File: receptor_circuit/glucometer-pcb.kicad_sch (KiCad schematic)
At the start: 22 parts, among them IC1 RC4558IP, IC2 LM1458N, IC3 RC4558IP, U1 ESP32_DevKit_V1_DOIT

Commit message: change name
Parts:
- removed BZ1: Buzzer, Buzzer_Beeper:MagneticBuzzer_Kingstate_KCG0601, symbol Device:Buzzer
- removed D1: LED, LED_THT:LED_D3.0mm_Clear, symbol Device:LED
- removed D2: LED, LED_THT:LED_D3.0mm_FlatTop, symbol Device:LED
- removed R3: 120, Resistor_THT:R_Axial_DIN0204_L3.6mm_D1.6mm_P7.62mm_Horizontal, symbol Device:R
- removed R4: 240, Resistor_THT:R_Axial_DIN0204_L3.6mm_D1.6mm_P7.62mm_Horizontal, symbol Device:R
- removed U1: ESP32_DevKit_V1_DOIT, esp32_devkit_v1_doit:esp32_devkit_v1_doit, symbol esp32_devkit_v1_doit:ESP32_DevKit_V1_DOIT
- added TP3: (no value), TestPoint:TestPoint_Keystone_5015_Micro-Minature, symbol Connector:TestPoint
- renumbered D3 to D1, R5 to R3, R6 to R4, R7 to R5, R8 to R6, R9 to R7
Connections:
- net SIGNAL_OUT: no longer names the net of IC3.6 (2IN-), R6.1, R7.2
- net SIGNAL_OUT: now also TP3.1

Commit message: fixed PCB
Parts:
- LM1458N1: renamed from IC2; value LM1458N -> (none)
- S_OUT1: renamed from TP3; footprint TestPoint:TestPoint_Keystone_5015_Micro-Minature -> (none)
- renumbered C2 to C1, C3 to C2, C1 to C3, TP1 to GND1, R4 to R1, R5 to R2, R1 to R3, R2 to R4, R3 to R5, IC1 to RC4558IP1, IC3 to RC4558IP2, D1 to RECEPTOR_DIODE1, TP2 to VCC1
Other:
- moved on the sheet: C1, C2, C3, GND1, LM1458N1, R1, R2, R3, R4, R5, R6, R7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

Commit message: receptor footprint update
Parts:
- LM1458N1: value (none) -> LM1458N
- RECEPTOR_DIODE1: footprint LED_SMD:LED_2010_5025Metric -> (none)
- S_OUT1: value (none) -> SIGNAL_OUT; footprint (none) -> TestPoint:TestPoint_Keystone_5015_Micro-Minature
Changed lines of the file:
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@@
       (effects (font (size 1.27 1.27)) (justify left))
     )
-    (property "Value" "" (id 1) (at 270.8694 62.425 90)
-      (effects (font (size 1.27 1.27)) (justify left))
-    )
-    (property "Footprint" "" (id 2) (at 265.7894 66.2351 0)
+    (property "Value" "SIGNAL_OUT" (id 1) (at 270.8694 62.425 90)
+      (effects (font (size 1.27 1.27)) (justify left))
+    )
+    (property "Footprint" "TestPoint:TestPoint_Keystone_5015_Micro-Minature" (id 2) (at 265.7894 66.2351 0)
       (effects (font (size 1.27 1.27)) hide)
     )
@@
     (in_bom yes) (on_board yes) (fields_autoplaced)
     (property "Reference" "LM1458N1" (id 0) (at 76.2 58.42 0))
-    (property "Value" "" (id 1) (at 76.2 60.96 0))
+    (property "Value" "LM1458N" (id 1) (at 76.2 60.96 0))
     (property "Footprint" "Custom:MC1458N" (id 2) (at 107.95 63.5 0)
       (effects (font (size 1.27 1.27)) (justify left) hide)
@@
       (effects (font (size 1.27 1.27)) (justify right))
     )
-    (property "Footprint" "LED_SMD:LED_2010_5025Metric" (id 2) (at 17.78 50.8 0)
+    (property "Footprint" "" (id 2) (at 17.78 50.8 0)
       (effects (font (size 1.27 1.27)) hide)
     )
@@
     )
     (path "/e278b743-dbab-45ed-8e87-8cb90b916702"
-      (reference "RECEPTOR_DIODE1") (unit 1) (value "D_Photo") (footprint "LED_SMD:LED_2010_5025Metric")
+      (reference "RECEPTOR_DIODE1") (unit 1) (value "D_Photo") (footprint "LED_SMD:LED_2512_6332Metric")
     )
     (path "/34600403-f41d-47ed-8742-771add37111a"

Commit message: updated footprints
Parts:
- C1: value 15p -> (none); footprint Capacitor_THT:CP_Radial_D8.0mm_P3.80mm -> (none)
- C2: value 100n -> (none); footprint Capacitor_THT:CP_Radial_Tantal_D7.0mm_P5.00mm -> (none)
- C3: value 10u -> (none); footprint Capacitor_THT:CP_Radial_Tantal_D7.0mm_P5.00mm -> (none)
- RECEPTOR_DIODE1: footprint (none) -> LED_SMD:LED_2512_6332Metric
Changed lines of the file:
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@@
     (in_bom yes) (on_board yes) (fields_autoplaced)
     (property "Reference" "C3" (id 0) (at 175.337 120.1313 90))
-    (property "Value" "10u" (id 1) (at 175.337 122.6713 90))
-    (property "Footprint" "Capacitor_THT:CP_Radial_Tantal_D7.0mm_P5.00mm" (id 2) (at 179.147 126.7861 0)
+    (property "Value" "" (id 1) (at 175.337 122.6713 90))
+    (property "Footprint" "" (id 2) (at 179.147 126.7861 0)
       (effects (font (size 1.27 1.27)) hide)
     )
@@
     (in_bom yes) (on_board yes) (fields_autoplaced)
     (property "Reference" "C1" (id 0) (at 44.45 24.13 90))
-    (property "Value" "15p" (id 1) (at 44.45 26.67 90))
-    (property "Footprint" "Capacitor_THT:CP_Radial_D8.0mm_P3.80mm" (id 2) (at 48.26 30.7848 0)
+    (property "Value" "" (id 1) (at 44.45 26.67 90))
+    (property "Footprint" "" (id 2) (at 48.26 30.7848 0)
       (effects (font (size 1.27 1.27)) hide)
     )
@@
       (effects (font (size 1.27 1.27)) (justify right))
     )
-    (property "Value" "100n" (id 1) (at 85.09 31.7499 0)
+    (property "Value" "" (id 1) (at 85.09 31.7499 0)
       (effects (font (size 1.27 1.27)) (justify right))
     )
-    (property "Footprint" "Capacitor_THT:CP_Radial_Tantal_D7.0mm_P5.00mm" (id 2) (at 107.95 25.4 0)
+    (property "Footprint" "" (id 2) (at 107.95 25.4 0)
       (effects (font (size 1.27 1.27)) hide)
     )
@@
       (effects (font (size 1.27 1.27)) (justify right))
     )
-    (property "Footprint" "" (id 2) (at 17.78 50.8 0)
+    (property "Footprint" "LED_SMD:LED_2512_6332Metric" (id 2) (at 17.78 50.8 0)
       (effects (font (size 1.27 1.27)) hide)
     )
@@
     )
     (path "/6e51d59d-a712-422e-a594-3a08db72143f"
-      (reference "C1") (unit 1) (value "15p") (footprint "Capacitor_THT:CP_Radial_D8.0mm_P3.80mm")
+      (reference "C1") (unit 1) (value "15p") (footprint "Capacitor_THT:C_Disc_D4.3mm_W1.9mm_P5.00mm")
     )
     (path "/8777605c-db0c-4cf4-9b07-6eb49a9a4f9e"
-      (reference "C2") (unit 1) (value "100n") (footprint "Capacitor_THT:CP_Radial_Tantal_D7.0mm_P5.00mm")
+      (reference "C2") (unit 1) (value "100n") (footprint "Capacitor_THT:C_Disc_D4.3mm_W1.9mm_P5.00mm")
     )
     (path "/4a7b0df0-d7d6-445b-b3ac-9e0367190cc3"
-      (reference "C3") (unit 1) (value "10u") (footprint "Capacitor_THT:CP_Radial_Tantal_D7.0mm_P5.00mm")
+      (reference "C3") (unit 1) (value "10u") (footprint "Capacitor_THT:C_Disc_D4.3mm_W1.9mm_P5.00mm")
     )
     (path "/c1089e62-6a3d-4c09-9cdd-b0398d606cc7"

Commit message: .
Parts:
- C1: value (none) -> 15p; footprint (none) -> Capacitor_THT:C_Disc_D4.3mm_W1.9mm_P5.00mm
- C2: value (none) -> 100n; footprint (none) -> Capacitor_THT:C_Disc_D4.3mm_W1.9mm_P5.00mm
- C3: footprint (none) -> Capacitor_THT:C_Disc_D4.3mm_W1.9mm_P5.00mm
- R5: value 25k -> (none); footprint Resistor_THT:R_Axial_DIN0204_L3.6mm_D1.6mm_P7.62mm_Horizontal -> (none)
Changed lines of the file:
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@@
   (symbol (lib_id "Device:C") (at 175.337 127.7513 90) (unit 1)
     (in_bom yes) (on_board yes) (fields_autoplaced)
-    (property "Reference" "C3" (id 0) (at 175.337 120.1313 90))
-    (property "Value" "" (id 1) (at 175.337 122.6713 90))
-    (property "Footprint" "" (id 2) (at 179.147 126.7861 0)
+    (property "Reference" "C3" (id 0) (at 175.337 120.65 90))
+    (property "Value" "" (id 1) (at 175.337 123.19 90))
+    (property "Footprint" "Capacitor_THT:C_Disc_D4.3mm_W1.9mm_P5.00mm" (id 2) (at 179.147 126.7861 0)
       (effects (font (size 1.27 1.27)) hide)
     )
@@
       (effects (font (size 1.27 1.27)) (justify left))
     )
-    (property "Value" "25k" (id 1) (at 190.577 141.7212 0)
-      (effects (font (size 1.27 1.27)) (justify left))
-    )
-    (property "Footprint" "Resistor_THT:R_Axial_DIN0204_L3.6mm_D1.6mm_P7.62mm_Horizontal" (id 2) (at 186.259 140.4513 90)
+    (property "Value" "" (id 1) (at 190.577 141.7212 0)
+      (effects (font (size 1.27 1.27)) (justify left))
+    )
+    (property "Footprint" "" (id 2) (at 186.259 140.4513 90)
       (effects (font (size 1.27 1.27)) hide)
     )
@@
     (in_bom yes) (on_board yes) (fields_autoplaced)
     (property "Reference" "C1" (id 0) (at 44.45 24.13 90))
-    (property "Value" "" (id 1) (at 44.45 26.67 90))
-    (property "Footprint" "" (id 2) (at 48.26 30.7848 0)
+    (property "Value" "15p" (id 1) (at 44.45 26.67 90))
+    (property "Footprint" "Capacitor_THT:C_Disc_D4.3mm_W1.9mm_P5.00mm" (id 2) (at 48.26 30.7848 0)
       (effects (font (size 1.27 1.27)) hide)
     )
@@
       (effects (font (size 1.27 1.27)) (justify right))
     )
-    (property "Value" "" (id 1) (at 85.09 31.7499 0)
+    (property "Value" "100n" (id 1) (at 85.09 31.7499 0)
       (effects (font (size 1.27 1.27)) (justify right))
     )
-    (property "Footprint" "" (id 2) (at 107.95 25.4 0)
+    (property "Footprint" "Capacitor_THT:C_Disc_D4.3mm_W1.9mm_P5.00mm" (id 2) (at 107.95 25.4 0)
       (effects (font (size 1.27 1.27)) hide)
     )
@@
     )
     (path "/4a7b0df0-d7d6-445b-b3ac-9e0367190cc3"
-      (reference "C3") (unit 1) (value "10u") (footprint "Capacitor_THT:C_Disc_D4.3mm_W1.9mm_P5.00mm")
+      (reference "C3") (unit 1) (value "1u") (footprint "Capacitor_THT:C_Disc_D4.3mm_W1.9mm_P5.00mm")
     )
     (path "/c1089e62-6a3d-4c09-9cdd-b0398d606cc7"
@@
     )
     (path "/5e1aeaac-5127-4872-a12f-e8e4419955ab"
-      (reference "R5") (unit 1) (value "25k") (footprint "Resistor_THT:R_Axial_DIN0204_L3.6mm_D1.6mm_P7.62mm_Horizontal")
+      (reference "R5") (unit 1) (value "300k") (footprint "Resistor_THT:R_Axial_DIN0204_L3.6mm_D1.6mm_P7.62mm_Horizontal")
     )
     (path "/21328896-da89-4b46-b5e9-10fe97839bf4"

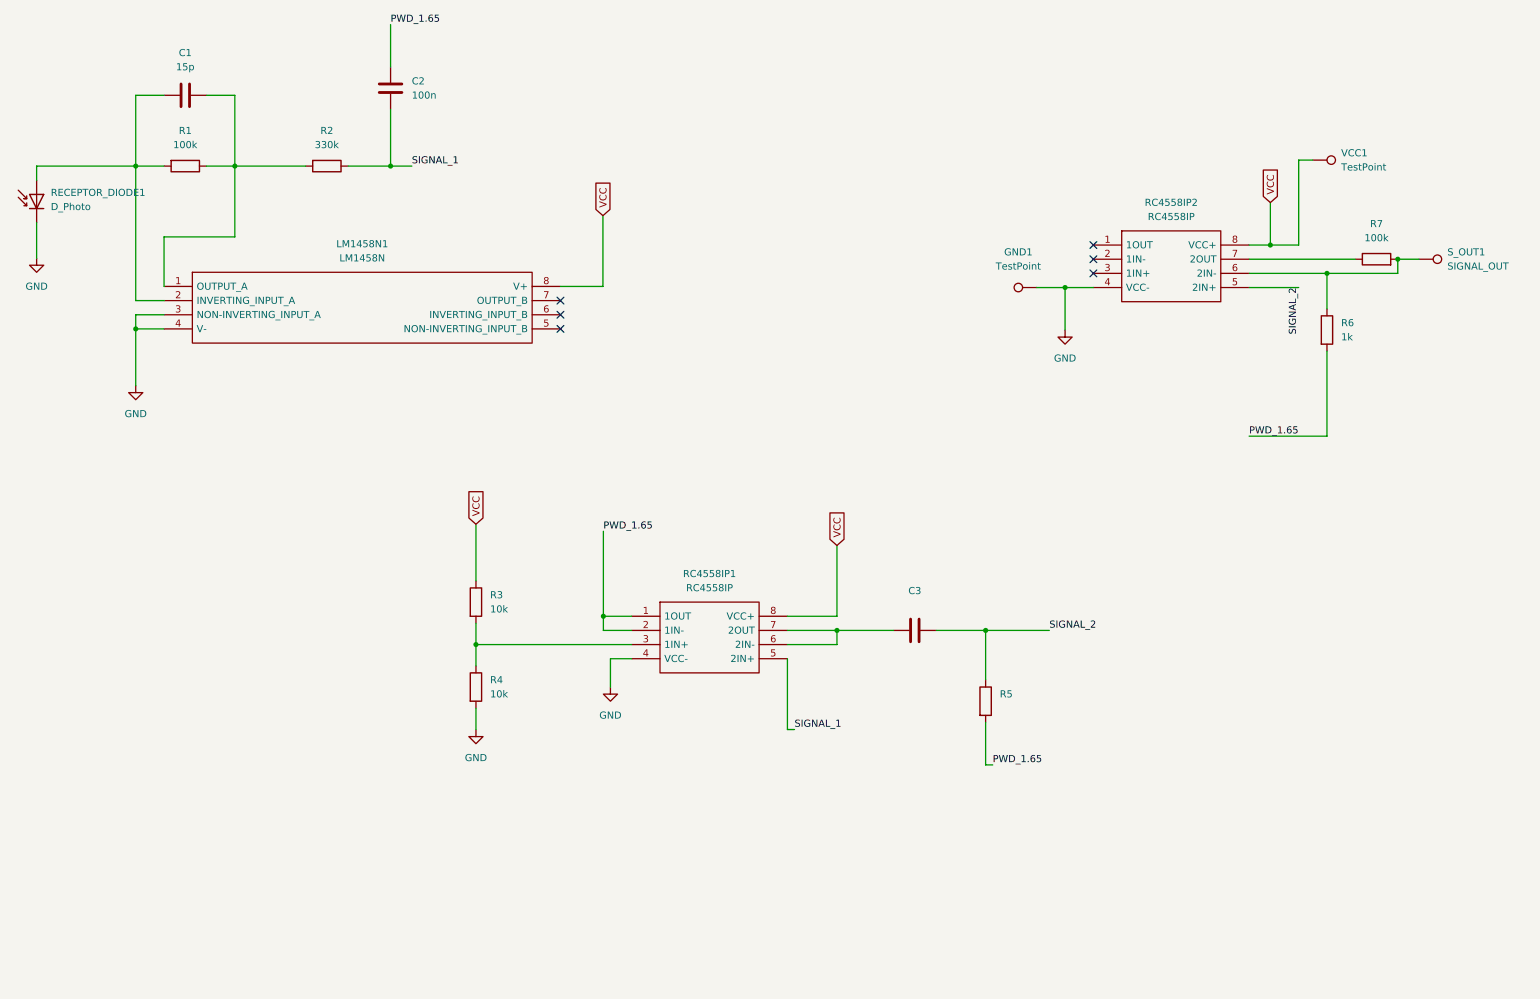
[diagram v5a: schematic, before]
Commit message: updated pcb pads
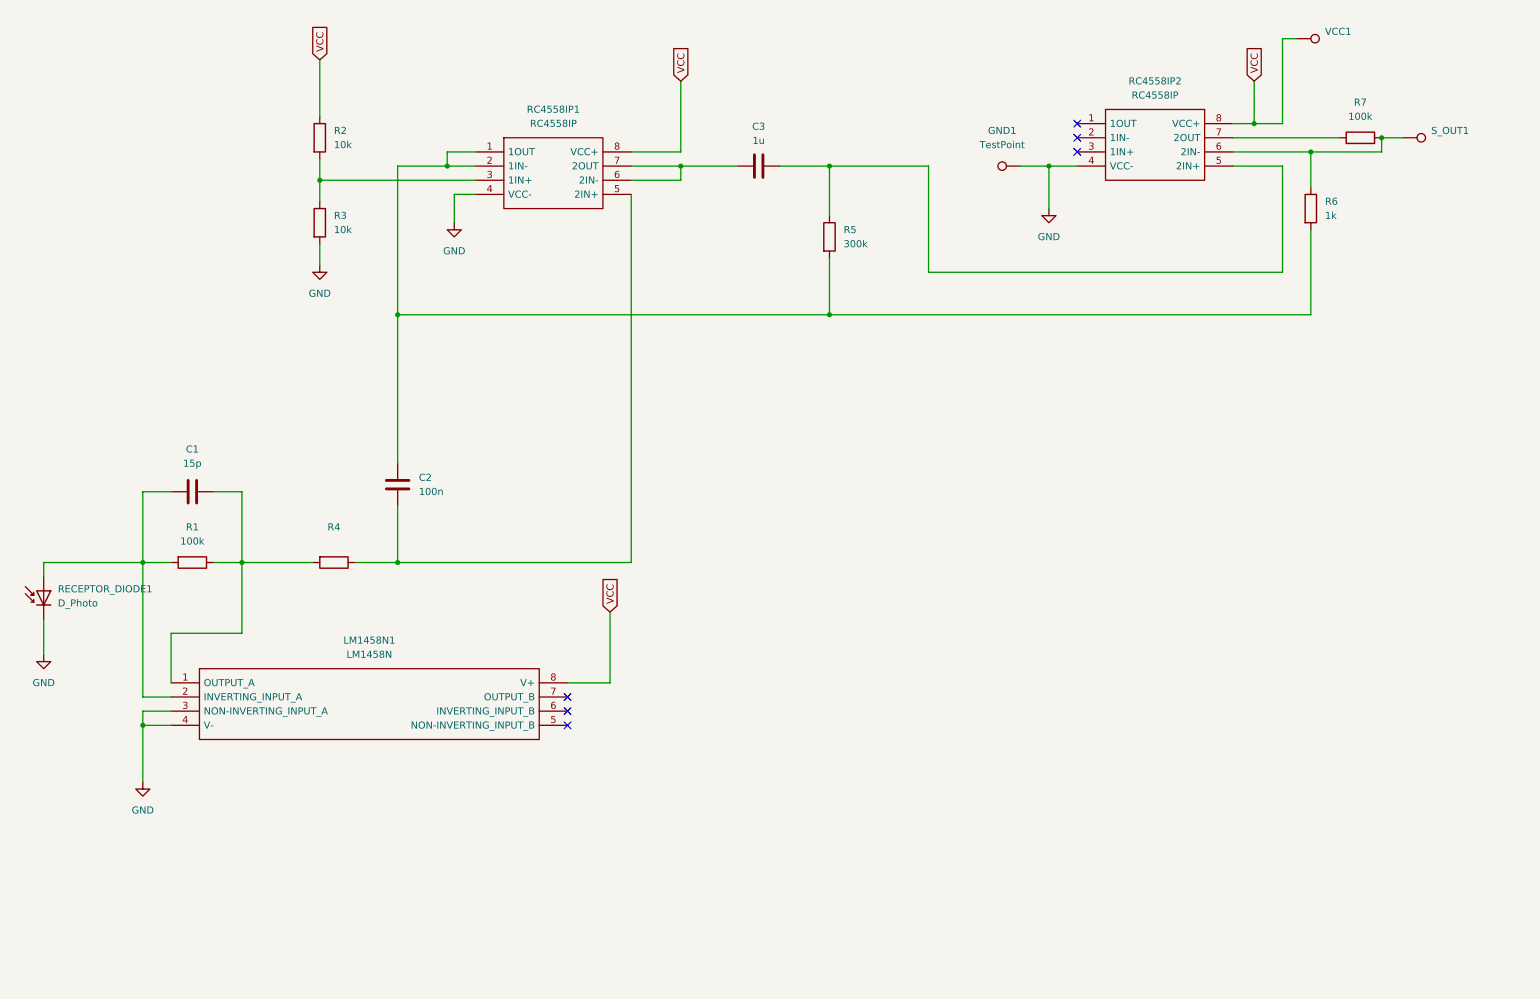
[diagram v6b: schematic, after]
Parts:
- C3: value (none) -> 1u
- R4: renamed from R2; value 330k -> (none)
- R5: value (none) -> 300k; footprint (none) -> Resistor_THT:R_Axial_DIN0204_L3.6mm_D1.6mm_P7.62mm_Horizontal
- S_OUT1: value SIGNAL_OUT -> (none)
- VCC1: value TestPoint -> (none)
- renumbered R3 to R2, R4 to R3
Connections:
- net PWD_1.65: no longer names the net of C2.2, R5.2, R6.2, RC4558IP1.1 (1OUT), RC4558IP1.2 (1IN-)
- net SIGNAL_1: no longer names the net of C2.1, R4.1, RC4558IP1.5 (2IN+)
- net SIGNAL_2: no longer names the net of C3.2, R5.1, RC4558IP2.5 (2IN+)
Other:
- moved on the sheet: C1, C2, C3, GND1, LM1458N1, R1, R2, R3, R4, R5, R6, R7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

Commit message: updated PCBs
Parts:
- R4: value (none) -> 300k
- S_OUT1, VCC1: value (none) -> TestPoint
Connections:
- net at R6.1, R7.2, RC4558IP2.6 (2IN-): no longer S_OUT1.1
- net at R7.1, RC4558IP2.7 (2OUT): now also S_OUT1.1
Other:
- moved on the sheet: R7
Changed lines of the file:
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@@
   (junction (at 160.02 71.12) (diameter 0) (color 0 0 0 0)
   )
+  (junction (at 199.39 44.45) (diameter 0) (color 0 0 0 0)
+  )
+  (junction (at 82.55 71.12) (diameter 0) (color 0 0 0 0)
+  )
   (junction (at 246.38 41.91) (diameter 0) (color 0 0 0 0)
   )
-  (junction (at 199.39 44.45) (diameter 0) (color 0 0 0 0)
-  )
-  (junction (at 82.55 71.12) (diameter 0) (color 0 0 0 0)
-  )
   (junction (at 91.44 44.45) (diameter 0) (color 0 0 0 0)
   )
@@
   (junction (at 82.55 115.57) (diameter 0) (color 0 0 0 0)
   )
+  (junction (at 259.08 39.37) (diameter 0) (color 0 0 0 0)
+  )
   (junction (at 68.58 46.99) (diameter 0) (color 0 0 0 0)
   )
   (junction (at 133.35 44.45) (diameter 0) (color 0 0 0 0)
-  )
-  (junction (at 259.08 39.37) (diameter 0) (color 0 0 0 0)
   )
   (junction (at 36.83 144.78) (diameter 0) (color 0 0 0 0)
@@
     (stroke (width 0) (type default) (color 0 0 0 0))
   )
+  (wire (pts (xy 256.54 41.91) (xy 259.08 41.91))
+    (stroke (width 0) (type default) (color 0 0 0 0))
+  )
   (wire (pts (xy 92.71 49.53) (xy 96.52 49.53))
     (stroke (width 0) (type default) (color 0 0 0 0))
@@
     (stroke (width 0) (type default) (color 0 0 0 0))
   )
-  (wire (pts (xy 246.38 41.91) (xy 259.08 41.91))
-    (stroke (width 0) (type default) (color 0 0 0 0))
-  )
   (wire (pts (xy 68.58 58.42) (xy 68.58 62.23))
     (stroke (width 0) (type default) (color 0 0 0 0))
@@
     (stroke (width 0) (type default) (color 0 0 0 0))
   )
+  (wire (pts (xy 246.38 41.91) (xy 248.92 41.91))
+    (stroke (width 0) (type default) (color 0 0 0 0))
+  )
   (wire (pts (xy 82.55 71.12) (xy 82.55 97.79))
     (stroke (width 0) (type default) (color 0 0 0 0))
@@
     (stroke (width 0) (type default) (color 0 0 0 0))
   )
-  (wire (pts (xy 232.41 39.37) (xy 251.46 39.37))
-    (stroke (width 0) (type default) (color 0 0 0 0))
-  )
   (wire (pts (xy 241.3 63.5) (xy 177.8 63.5))
     (stroke (width 0) (type default) (color 0 0 0 0))
@@
   )
   (wire (pts (xy 49.53 115.57) (xy 54.61 115.57))
+    (stroke (width 0) (type default) (color 0 0 0 0))
+  )
+  (wire (pts (xy 232.41 39.37) (xy 259.08 39.37))
     (stroke (width 0) (type default) (color 0 0 0 0))
   )
@@
       (effects (font (size 1.27 1.27)) (justify left))
     )
-    (property "Value" "" (id 1) (at 248.92 22.8599 90)
+    (property "Value" "TestPoint" (id 1) (at 248.92 22.8599 90)
       (effects (font (size 1.27 1.27)) (justify left))
     )
@@
       (effects (font (size 1.27 1.27)) (justify left))
     )
-    (property "Value" "" (id 1) (at 267.97 40.6399 90)
+    (property "Value" "TestPoint" (id 1) (at 267.97 40.6399 90)
       (effects (font (size 1.27 1.27)) (justify left))
     )
@@
     (in_bom yes) (on_board yes) (fields_autoplaced)
     (property "Reference" "R4" (id 0) (at 71.12 109.22 90))
-    (property "Value" "" (id 1) (at 71.12 111.76 90))
+    (property "Value" "300k" (id 1) (at 71.12 111.76 90))
     (property "Footprint" "Resistor_THT:R_Axial_DIN0204_L3.6mm_D1.6mm_P7.62mm_Horizontal" (id 2) (at 71.12 113.792 90)
       (effects (font (size 1.27 1.27)) hide)
@@
     (pin "8")
   )
-  (symbol (lib_id "Device:R") (at 255.27 39.37 90) (unit 1)
-    (in_bom yes) (on_board yes) (fields_autoplaced)
-    (property "Reference" "R7" (id 0) (at 255.27 33.02 90))
-    (property "Value" "100k" (id 1) (at 255.27 35.56 90))
-    (property "Footprint" "Resistor_THT:R_Axial_DIN0204_L3.6mm_D1.6mm_P7.62mm_Horizontal" (id 2) (at 255.27 41.148 90)
-      (effects (font (size 1.27 1.27)) hide)
-    )
-    (property "Datasheet" "~" (id 3) (at 255.27 39.37 0)
-      (effects (font (size 1.27 1.27)) hide)
-    )
+  (symbol (lib_id "Device:R") (at 252.73 41.91 270) (unit 1)
+    (in_bom yes) (on_board yes) (fields_autoplaced)
+    (property "Reference" "R7" (id 0) (at 252.73 35.56 90))
+    (property "Value" "100k" (id 1) (at 252.73 38.1 90))
+    (property "Footprint" "Resistor_THT:R_Axial_DIN0204_L3.6mm_D1.6mm_P7.62mm_Horizontal" (id 2) (at 252.73 40.132 90)
+      (effects (font (size 1.27 1.27)) hide)
+    )
+    (property "Datasheet" "~" (id 3) (at 252.73 41.91 0)
+      (effects (font (size 1.27 1.27)) hide)
+    )

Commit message: small changes and (temp V divisor)
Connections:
- net 1V6: now reaches C2.2, R5.2, R6.2, RC4558IP1.1 (1OUT), RC4558IP1.2 (1IN-)
- net SIGNAL_2: now reaches C3.2, R5.1, RC4558IP2.5 (2IN+)
- net SIGNAL_1: now reaches C2.1, R4.1, RC4558IP1.5 (2IN+)
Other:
- moved on the sheet: C1, C2, C3, GND1, LM1458N1, R1, R2, R3, R4, R5, R6, R7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
